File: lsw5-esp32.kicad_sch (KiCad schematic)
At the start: 40 parts, among them J1 Conn_02x03_Odd_Even, J2 Conn_01x04_Pin, J3 USB4105-GF-A, J4 Conn_02x05_Odd_Even, J6 Conn_01x04, Q1 AO3407A, U1 ESP32-S3-WROOM-1U, U2 LD1117S33TR_SOT223, U3 ISO1410DWR

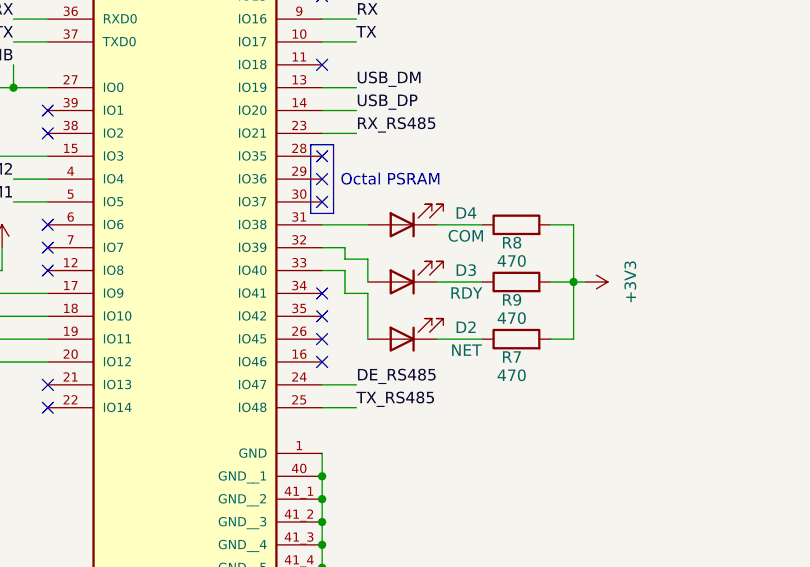
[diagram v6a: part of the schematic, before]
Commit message: Fix backwards LED (aka silkscreen)
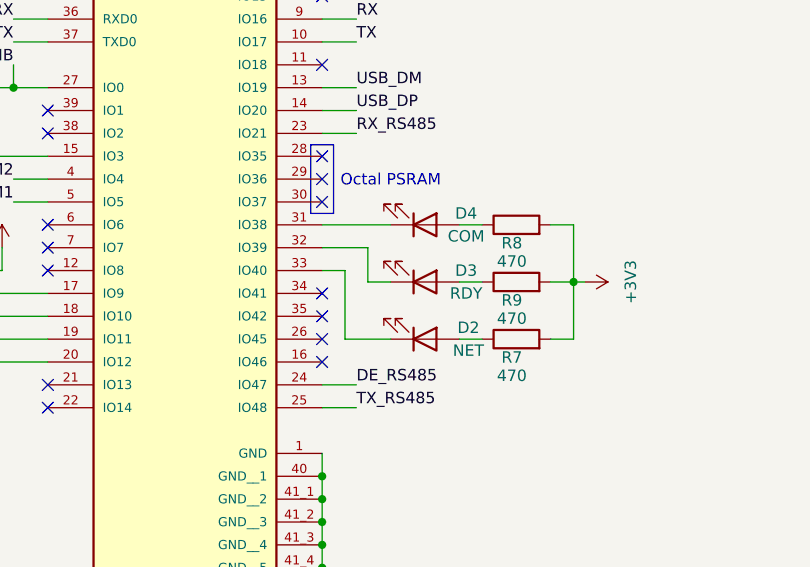
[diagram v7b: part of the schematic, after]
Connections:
- net at D4.1 (K): now also U1.31 (IO38); no longer R8.1
- net at D4.2 (A): now also R8.1; no longer U1.31 (IO38)
- net at R7.1: now also D2.2 (A); no longer D2.1 (K)
- net at U1.33 (IO40): now also D2.1 (K); no longer D2.2 (A)
- net at R9.1: now also D3.2 (A); no longer D3.1 (K)
- net at U1.32 (IO39): now also D3.1 (K); no longer D3.2 (A)
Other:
- moved on the sheet: D2, D3, D4
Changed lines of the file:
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@@
 	(wire
 		(pts
-			(xy 80.01 88.9) (xy 80.01 83.82)
-		)
-		(stroke
-			(width 0)
-			(type default)
-		)
-	)
-	(wire
-		(pts
 			(xy 78.74 124.46) (xy 78.74 130.81)
 		)
@@
 	(wire
 		(pts
-			(xy 80.01 83.82) (xy 77.47 83.82)
-		)
-		(stroke
-			(width 0)
-			(type default)
-		)
-	)
-	(wire
-		(pts
 			(xy 40.64 53.34) (xy 44.45 53.34)
 		)
@@
 	(wire
 		(pts
-			(xy 77.47 80.01) (xy 80.01 80.01)
-		)
-		(stroke
-			(width 0)
-			(type default)
-		)
-	)
-	(wire
-		(pts
 			(xy 17.78 68.58) (xy 22.86 68.58)
 		)
@@
 	(wire
 		(pts
-			(xy 87.63 76.2) (xy 92.71 76.2)
+			(xy 90.17 76.2) (xy 92.71 76.2)
 		)
 		(stroke
@@
 	(wire
 		(pts
-			(xy 80.01 80.01) (xy 80.01 82.55)
+			(xy 80.01 78.74) (xy 80.01 82.55)
 		)
 		(stroke
@@
 	(wire
 		(pts
-			(xy 74.93 76.2) (xy 80.01 76.2)
+			(xy 74.93 76.2) (xy 82.55 76.2)
 		)
 		(stroke
@@
 	(wire
 		(pts
-			(xy 74.93 78.74) (xy 77.47 78.74)
+			(xy 74.93 78.74) (xy 80.01 78.74)
 		)
 		(stroke
@@
 	(wire
 		(pts
+			(xy 80.01 82.55) (xy 82.55 82.55)
+		)
+		(stroke
+			(width 0)
+			(type default)
+		)
+	)
+	(wire
+		(pts
 			(xy 168.91 139.7) (xy 173.99 139.7)
 		)
@@
 	(wire
 		(pts
+			(xy 77.47 88.9) (xy 82.55 88.9)
+		)
+		(stroke
+			(width 0)
+			(type default)
+		)
+	)
+	(wire
+		(pts
 			(xy 186.69 25.4) (xy 186.69 30.48)
 		)
@@
 	(wire
 		(pts
-			(xy 77.47 80.01) (xy 77.47 78.74)
-		)
-		(stroke
-			(width 0)
-			(type default)
-		)
-	)
-	(wire
-		(pts
 			(xy 30.48 60.96) (xy 40.64 60.96)
 		)
@@
 	(wire
 		(pts
-			(xy 87.63 82.55) (xy 92.71 82.55)
+			(xy 90.17 82.55) (xy 92.71 82.55)
 		)
 		(stroke
@@
 	(wire
 		(pts
-			(xy 77.47 83.82) (xy 77.47 81.28)
+			(xy 77.47 81.28) (xy 77.47 88.9)
 		)
 		(stroke
@@
 	(wire
 		(pts
-			(xy 87.63 88.9) (xy 92.71 88.9)
+			(xy 90.17 88.9) (xy 92.71 88.9)
 		)
 		(stroke
@@
 	(symbol
 		(lib_id "Device:LED")
-		(at 83.82 76.2 180)
+		(at 86.36 76.2 0)
+		(mirror x)
 		(unit 1)
 		(exclude_from_sim no)
@@
 		)
 		(property "Footprint" "LED_SMD:LED_0603_1608Metric_Pad1.05x0.95mm_HandSolder"
-			(at 83.82 76.2 0)
+			(at 86.36 76.2 0)
 			(effects
 				(font
@@
 		)
 		(property "Datasheet" "~"
-			(at 83.82 76.2 0)
+			(at 86.36 76.2 0)
 			(effects
 				(font
@@
 		)
 		(property "Description" "Light emitting diode"
-			(at 83.82 76.2 0)
+			(at 86.36 76.2 0)
 			(effects
 				(font
@@
 		)
 		(property "Sim.Pins" "1=K 2=A"
-			(at 83.82 76.2 0)
+			(at 86.36 76.2 0)
 			(effects
 				(font
@@
 	(symbol
 		(lib_id "Device:LED")
-		(at 83.82 88.9 180)
+		(at 86.36 88.9 0)
+		(mirror x)
 		(unit 1)
 		(exclude_from_sim no)
@@
 		(dnp no)
 		(property "Reference" "D2"
-			(at 90.932 87.63 0)
+			(at 91.186 87.63 0)
 			(effects
 				(font
@@
 		)
 		(property "Value" "NET"
-			(at 90.932 90.17 0)
+			(at 91.186 90.17 0)
 			(effects
 				(font
@@
 		)
 		(property "Footprint" "LED_SMD:LED_0603_1608Metric_Pad1.05x0.95mm_HandSolder"
-			(at 83.82 88.9 0)
+			(at 86.36 88.9 0)
 			(effects
 				(font
@@
 		)
 		(property "Datasheet" "~"
-			(at 83.82 88.9 0)
+			(at 86.36 88.9 0)
 			(effects
 				(font
@@
 		)
 		(property "Description" "Light emitting diode"
-			(at 83.82 88.9 0)
+			(at 86.36 88.9 0)
 			(effects
 				(font
@@
 		)
 		(property "Sim.Pins" "1=K 2=A"
-			(at 83.82 88.9 0)
+			(at 86.36 88.9 0)
 			(effects
 				(font
@@
 	(symbol
 		(lib_id "Device:LED")
-		(at 83.82 82.55 180)
+		(at 86.36 82.55 0)
+		(mirror x)
 		(unit 1)
 		(exclude_from_sim no)
@@
 		)
 		(property "Footprint" "LED_SMD:LED_0603_1608Metric_Pad1.05x0.95mm_HandSolder"
-			(at 83.82 82.55 0)
+			(at 86.36 82.55 0)
 			(effects
 				(font
@@
 		)
 		(property "Datasheet" "~"
-			(at 83.82 82.55 0)
+			(at 86.36 82.55 0)
 			(effects
 				(font
@@
 		)
 		(property "Description" "Light emitting diode"
-			(at 83.82 82.55 0)
+			(at 86.36 82.55 0)
 			(effects
 				(font
@@
 		)
 		(property "Sim.Pins" "1=K 2=A"
-			(at 83.82 82.55 0)
+			(at 86.36 82.55 0)
 			(effects
 				(font
